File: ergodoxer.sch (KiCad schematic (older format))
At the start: 106 parts, among them J1 USB_C_Receptacle, SW1 SW_Push, SW10 SW_Push, SW11 SW_Push, SW12 SW_Push, SW13 SW_Push, SW14 SW_Push, SW15 SW_Push, SW16 SW_Push, SW17 SW_Push, SW18 SW_Push, SW19 SW_Push, SW2 SW_Push, SW20 SW_Push, SW21 SW_Push, SW22 SW_Push, SW23 SW_Push, SW24 SW_Push, SW25 SW_Push, SW26 SW_Push, SW27 SW_Push, SW28 SW_Push, SW29 SW_Push, SW3 SW_Push, SW30 SW_Push, SW31 SW_Push, SW32 SW_Push, SW33 SW_Push, SW34 SW_Push, SW35 SW_Push, SW36 SW_Push, SW37 SW_Push, SW38 SW_Push, SW39 SW_Push, SW4 SW_Push, SW40 SW_Push, SW41 SW_Push, SW43 SW_Push, SW44 SW_Push, SW45 SW_Push, SW46 SW_Push, SW47 SW_Push, SW48 SW_Push, SW49 SW_Push, SW5 SW_Push, SW50 SW_Push, SW51 SW_Push, SW52 SW_Push, SW53 SW_Push, SW6 SW_Push, SW7 SW_Push, SW8 SW_Push, SW9 SW_Push, U1 proton_c

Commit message: Flip switches upside down
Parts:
- SW1, SW10, SW11, SW12, SW13, SW14, SW15, SW16, SW17, SW18, SW19, SW2, SW20, SW21, SW22, SW23, SW24, SW25, SW26, SW27, SW28, SW29, SW3, SW30, SW31, SW32, SW33, SW34, SW35, SW36, SW37, SW38, SW39, SW4, SW40, SW41, SW43, SW44, SW45, SW46, SW47, SW48, SW49, SW5, SW50, SW51, SW52, SW53, SW6, SW7, SW8, SW9: footprint Button_Switch_keyboard:SW_Cherry_MX_1.00u_PCB -> switches:SW_Cherry_MX_1.00u_PCB_dual
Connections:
- no-connect marks 0 -> 21

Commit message: Add leds
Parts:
- added LE23, LED1, LED10, LED11, LED12, LED13, LED14, LED15, LED16, LED17, LED18, LED19, LED2, LED20, LED21, LED22, LED24, LED25, LED26, LED27, LED28, LED29, LED3, LED30, LED31, LED32, LED33, LED34, LED35, LED36, LED37, LED38, LED39, LED4, LED40, LED41, LED45, LED46, LED47, LED48, LED49, LED5, LED50, LED51, LED52, LED53, LED6, LED7, LED8, LED9: WS2812B, switches:LED_WS2812B-inverted, symbol LED:WS2812B
- added LED43, LED44: WS2812, switches:LED_WS2812B-inverted, symbol LED:WS2812B
- SW1, SW13, SW19, SW25, SW31, SW37, SW7: value SW_Push -> SW_Push_mod
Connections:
- net GND: now also LE23.3 (VSS), LED1.3 (VSS), LED10.3 (VSS), LED11.3 (VSS), LED12.3 (VSS), LED13.3 (VSS), LED14.3 (VSS), LED15.3 (VSS), LED16.3 (VSS), LED17.3 (VSS), LED18.3 (VSS), LED19.3 (VSS), LED2.3 (VSS), LED20.3 (VSS), LED21.3 (VSS), LED22.3 (VSS), LED24.3 (VSS), LED25.3 (VSS), LED26.3 (VSS), LED27.3 (VSS), LED28.3 (VSS), LED29.3 (VSS), LED3.3 (VSS), LED30.3 (VSS), LED31.3 (VSS), LED32.3 (VSS), LED33.3 (VSS), LED34.3 (VSS), LED35.3 (VSS), LED36.3 (VSS), LED37.3 (VSS), LED38.3 (VSS), LED39.3 (VSS), LED4.3 (VSS), LED40.3 (VSS), LED41.3 (VSS), LED43.3 (VSS), LED44.3 (VSS), LED45.3 (VSS), LED46.3 (VSS), LED47.3 (VSS), LED48.3 (VSS), LED49.3 (VSS), LED5.3 (VSS), LED50.3 (VSS), LED51.3 (VSS), LED52.3 (VSS), LED53.3 (VSS), LED6.3 (VSS), LED7.3 (VSS), LED8.3 (VSS), LED9.3 (VSS)
- net VBUS: now also LE23.1 (VDD), LED1.1 (VDD), LED10.1 (VDD), LED11.1 (VDD), LED12.1 (VDD), LED13.1 (VDD), LED14.1 (VDD), LED15.1 (VDD), LED16.1 (VDD), LED17.1 (VDD), LED18.1 (VDD), LED19.1 (VDD), LED2.1 (VDD), LED20.1 (VDD), LED21.1 (VDD), LED22.1 (VDD), LED24.1 (VDD), LED25.1 (VDD), LED26.1 (VDD), LED27.1 (VDD), LED28.1 (VDD), LED29.1 (VDD), LED3.1 (VDD), LED30.1 (VDD), LED31.1 (VDD), LED32.1 (VDD), LED33.1 (VDD), LED34.1 (VDD), LED35.1 (VDD), LED36.1 (VDD), LED37.1 (VDD), LED38.1 (VDD), LED39.1 (VDD), LED4.1 (VDD), LED40.1 (VDD), LED41.1 (VDD), LED43.1 (VDD), LED44.1 (VDD), LED45.1 (VDD), LED46.1 (VDD), LED47.1 (VDD), LED48.1 (VDD), LED49.1 (VDD), LED5.1 (VDD), LED50.1 (VDD), LED51.1 (VDD), LED52.1 (VDD), LED53.1 (VDD), LED6.1 (VDD), LED7.1 (VDD), LED8.1 (VDD), LED9.1 (VDD)
- net column1: now also U1.B0 (PB0); no longer U1.B1 (PB1)
- net column2: now also U1.B1 (PB1); no longer U1.B2 (PB2)
- net column3: now also U1.B2 (PB2); no longer U1.B3 (PB3)
- net column4: now also U1.B13 (PB13/SCLK); no longer U1.B7 (PB7/SDA)
- net column5: now also SW43.1, SW44.1, U1.B5 (PB5); no longer U1.B6 (PB6/SCL)
- net column6: now also SW46.1, SW47.1, U1.B4 (PB4); no longer U1.B5 (PB5)
- net column7: now also SW48.1, SW49.1, SW50.1, U1.B3 (PB3); no longer U1.B4 (PB4)
- net column8: now also SW45.1, SW51.1, SW52.1, SW53.1, U1.B10 (PB10); no longer SW43.1, SW44.1, U1.A7 (PA7)
- net row4: no longer D45.1 (K), D48.1 (K), D51.1 (K)
- net row5: now also D45.1 (K), U1.A4 (PA4/SPEAKER1); no longer D43.1 (K), D46.1 (K), D49.1 (K), D52.1 (K), U1.B9 (PB9)
- net row6: now also D48.1 (K), D51.1 (K), U1.A5 (PA5/SPEAKER2); no longer D44.1 (K), D47.1 (K), D50.1 (K), D53.1 (K), U1.B11 (PB11)
- net row7: now reaches U1.B12 (PB12)
- net row7: now also D43.1 (K), D46.1 (K), D49.1 (K), D52.1 (K)
- net SDA: now reaches J1.A5 (CC1), J1.A8 (SBU1)
- net SDA: now also U1.B7 (PB7/SDA); no longer U1.B13 (PB13/SCLK)
- net SCL: now reaches J1.A6 (D+), J1.A7 (D-)
- net SCL: now also U1.B6 (PB6/SCL); no longer U1.B15 (PB15/MOSI)
- removed net column10: SW48.1, SW49.1, SW50.1, U1.A5 (PA5/SPEAKER2)
- removed net column11: SW51.1, SW52.1, SW53.1, U1.A4 (PA4/SPEAKER1)
- removed net column9: SW45.1, SW46.1, SW47.1, U1.A6 (PA6)
- new net: LED43.4 (DIN), LED44.2 (DOUT)
- new net: LED44.4 (DIN), LED47.2 (DOUT)
- new net: LED19.4 (DIN), LED25.2 (DOUT)
- new net: LED25.4 (DIN), LED31.2 (DOUT)
- new net: LED26.2 (DOUT), LED32.4 (DIN)
- new net: LED20.2 (DOUT), LED26.4 (DIN)
- new net: LED21.4 (DIN), LED27.2 (DOUT)
- new net: LED27.4 (DIN), LED33.2 (DOUT)
- new net: LE23.4 (DIN), LED29.2 (DOUT)
- new net: LED29.4 (DIN), LED35.2 (DOUT)
- new net: LED30.2 (DOUT), LED36.4 (DIN)
- new net: LED24.2 (DOUT), LED30.4 (DIN)
- new net: LED31.4 (DIN), LED37.2 (DOUT)
- new net: LED32.2 (DOUT), LED38.4 (DIN)
- new net: LED33.4 (DIN), LED39.2 (DOUT)
- new net: LED35.4 (DIN), LED41.2 (DOUT)
- new net: LED36.2 (DOUT), LED45.4 (DIN)
- new net: LED38.2 (DOUT), LED39.4 (DIN)
- new net: LED40.2 (DOUT), LED41.4 (DIN)
- new net: LED13.4 (DIN), LED19.2 (DOUT)
- new net: LED14.2 (DOUT), LED20.4 (DIN)
- new net: LED15.4 (DIN), LED21.2 (DOUT)
- new net: LE23.2 (DOUT), LED17.4 (DIN)
- new net: LED18.2 (DOUT), LED24.4 (DIN)
- new net: LED13.2 (DOUT), LED7.4 (DIN)
- new net: LED14.4 (DIN), LED8.2 (DOUT)
- new net: LED15.2 (DOUT), LED9.4 (DIN)
- new net: LED11.4 (DIN), LED17.2 (DOUT)
- new net: LED12.2 (DOUT), LED18.4 (DIN)
- new net: LED1.2 (DOUT), LED2.4 (DIN)
- new net: LED1.4 (DIN), LED7.2 (DOUT)
- new net: LED2.2 (DOUT), LED8.4 (DIN)
- new net: LED3.2 (DOUT), LED4.4 (DIN)
- new net: LED3.4 (DIN), LED9.2 (DOUT)
- new net: LED5.2 (DOUT), LED6.4 (DIN)
- new net: LED11.2 (DOUT), LED5.4 (DIN)
- new net: LED12.4 (DIN), LED6.2 (DOUT)
- new net: LED45.2 (DOUT), LED48.4 (DIN)
- new net: LED48.2 (DOUT), LED51.4 (DIN)
- new net: LED51.2 (DOUT), LED52.4 (DIN)
- new net: LED52.2 (DOUT), LED53.4 (DIN)
- new net: LED50.4 (DIN), LED53.2 (DOUT)
- new net: LED49.4 (DIN), LED50.2 (DOUT)
- new net: LED46.4 (DIN), LED49.2 (DOUT)
- new net: LED46.2 (DOUT), LED47.4 (DIN)
- new net LED_IN: U1.B15 (PB15/MOSI)
- new net ledinput: LED37.4 (DIN)
- new net row8: D44.1 (K), D47.1 (K), D50.1 (K), D53.1 (K), U1.B11 (PB11)
- now unconnected: J1.B6 (D+), J1.B7 (D-), U1.B14 (PB14/MISO)
- no-connect marks 21 -> 17
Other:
- moved on the sheet: D43, D44, D45, D46, D47, D48, D49, D50, D51, D52, D53, SW43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

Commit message: WIP update to square led holes
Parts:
- removed D36: 1N4148, Diodes_ThroughHole:D_DO-35_SOD27_P7.62mm_Horizontal, symbol Diode:1N4148
- removed LED36: WS2812B, switches:LED_WS2812B-inverted, symbol LED:WS2812B
- removed SW36: SW_Push, switches:SW_Cherry_MX_1.00u_PCB_dual, symbol Switch:SW_Push
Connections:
- net column6: now also SW45.1
- net column8: no longer SW45.1
- net row5: no longer D45.1 (K)
- net row6: now also D45.1 (K)
- net at LED28.2 (DOUT): now also LED34.4 (DIN)
- net at LED28.4 (DIN): now also LED22.2 (DOUT)
- net at LED30.2 (DOUT): now also LED45.4 (DIN)
- net at LED34.2 (DOUT): now also LED40.4 (DIN)
- net at LED22.4 (DIN): now also LED16.2 (DOUT)
- net at LED16.4 (DIN): now also LED10.2 (DOUT)
- net at LED4.2 (DOUT): now also LED10.4 (DIN)
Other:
- moved on the sheet: D45, SW45
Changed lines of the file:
@@
-	0    -1   -1   0
-$EndComp
-$Comp
-L Switch:SW_Push SW36
-U 1 1 5C72915C
-P 5450 5600
-F 0 "SW36" H 5450 5885 50  0000 C CNN
-F 1 "SW_Push" H 5450 5794 50  0000 C CNN
-F 2 "switches:SW_Cherry_MX_1.00u_PCB_dual" H 5450 5800 50  0001 C CNN
-F 3 "" H 5450 5800 50  0001 C CNN
-	1    5450 5600
-	1    0    0    -1
-$EndComp
-$Comp
-L Diode:1N4148 D36
-U 1 1 5C729163
-P 5650 5750
-F 0 "D36" H 5650 5850 50  0000 C CNN
-F 1 "1N4148" H 5650 5650 50  0000 C CNN
-F 2 "Diodes_ThroughHole:D_DO-35_SOD27_P7.62mm_Horizontal" H 5650 5575 50  0001 C CNN
-F 3 "http://www.nxp.com/documents/data_sheet/1N4148_1N4448.pdf" H 5650 5750 50  0001 C CNN
-	1    5650 5750
 	0    -1   -1   0
 $EndComp
@@
 Connection ~ 4250 5900
 Wire Wire Line
-	4950 5900 5650 5900
-Connection ~ 4950 5900
-Wire Wire Line
 	3150 4800 3150 5600
 Wire Wire Line
@@
 Wire Wire Line
 	4550 4800 4550 5600
-Wire Wire Line
-	5250 4800 5250 5600
 Wire Wire Line
 	2450 4800 2450 5600
@@
 Connection ~ 3850 4800
 Connection ~ 4550 4800
-Connection ~ 5250 4800
 $Comp
 L Switch:SW_Push SW45
 U 1 1 5C75EE71
-P 4700 6650
-F 0 "SW45" H 4700 6935 50  0000 C CNN
-F 1 "SW_Push" H 4700 6844 50  0000 C CNN
-F 2 "switches:SW_Cherry_MX_1.00u_PCB_dual" H 4700 6850 50  0001 C CNN
-F 3 "" H 4700 6850 50  0001 C CNN
-	1    4700 6650
+P 4700 6800
+F 0 "SW45" H 4700 7085 50  0000 C CNN
+F 1 "SW_Push" H 4700 6994 50  0000 C CNN
+F 2 "switches:SW_Cherry_MX_1.00u_PCB_dual" H 4700 7000 50  0001 C CNN
+F 3 "" H 4700 7000 50  0001 C CNN
+	1    4700 6800
 	1    0    0    -1
 $EndComp
@@
 L Diode:1N4148 D45
 U 1 1 5C75EE78
-P 4900 6800
-F 0 "D45" H 4900 6900 50  0000 C CNN
-F 1 "1N4148" H 4900 6700 50  0000 C CNN
-F 2 "Diodes_ThroughHole:D_DO-35_SOD27_P7.62mm_Horizontal" H 4900 6625 50  0001 C CNN
-F 3 "http://www.nxp.com/documents/data_sheet/1N4148_1N4448.pdf" H 4900 6800 50  0001 C CNN
-	1    4900 6800
+P 4900 6950
+F 0 "D45" H 4900 7050 50  0000 C CNN
+F 1 "1N4148" H 4900 6850 50  0000 C CNN
+F 2 "Diodes_ThroughHole:D_DO-35_SOD27_P7.62mm_Horizontal" H 4900 6775 50  0001 C CNN
+F 3 "http://www.nxp.com/documents/data_sheet/1N4148_1N4448.pdf" H 4900 6950 50  0001 C CNN
+	1    4900 6950
 	0    -1   -1   0
 $EndComp
@@
 row6
 Wire Wire Line
-	3500 7100 5600 7100
-Text GLabel 4500 7500 1    50   Input ~ 0
+	3500 7100 4900 7100
+Text GLabel 4500 6550 1    50   Input ~ 0
 column6
-Wire Wire Line
-	4500 7500 4500 7600
 Connection ~ 4500 7600
-Text GLabel 4500 6400 1    50   Input ~ 0
-column8
-Wire Wire Line
-	4500 6400 4500 6650
-Text GLabel 4450 6950 0    50   Input ~ 0
-row5
-Wire Wire Line
-	4450 6950 4900 6950
+Wire Wire Line
+	4500 6550 4500 6800
 Wire Wire Line
 	7950 3350 8100 3350
@@
 	1    -2800 4700
 	-1   0    0    1
-$EndComp
-$Comp
-L LED:WS2812B LED36
-U 1 1 5CDF1437
-P -2800 5750
-F 0 "LED36" H -2459 5796 50  0000 L CNN
-F 1 "WS2812B" H -2459 5705 50  0000 L CNN
-F 2 "switches:LED_WS2812B-inverted" H -2750 5450 50  0001 L TNN
-F 3 "https://cdn-shop.adafruit.com/datasheets/WS2812B.pdf" H -2700 5375 50  0001 L TNN
-	1    -2800 5750
-	1    0    0    -1
 $EndComp
 $Comp
@@
 	-4750 5750 -4300 5750
 Wire Wire Line
-	-3700 5750 -3100 5750
-Wire Wire Line
 	-1550 5000 -1550 5200
 Wire Wire Line
@@
 	-2800 5200 -4000 5200
 Wire Wire Line
-	-2800 5200 -2800 5450
-Wire Wire Line
 	-1550 3900 -1550 4100
 Wire Wire Line
@@
 Wire Wire Line
 	-9150 3600 -8950 3600
-Wire Wire Line
-	-2500 5750 -1550 5750
 $Comp
 L power:GND #PWR0107
@@
 	-8650 6450 -8650 6050
 Wire Wire Line
-	-2800 6050 -2800 6450
-Wire Wire Line
 	-7450 6050 -7450 6450
 Wire Wire Line
@@
 	-5050 6450 -4000 6450
 Connection ~ -4000 6450
-Wire Wire Line
-	-4000 6450 -2800 6450
 Wire Wire Line
 	-4000 6050 -4000 6450
@@
 Connection ~ 3800 7600
 $Comp
-L power:GND #PWR?
+L power:GND #PWR0128
 U 1 1 5C754416
-P -2800 6450
-F 0 "#PWR?" H -2800 6200 50  0001 C CNN
-F 1 "GND" V -2795 6322 50  0000 R CNN
-F 2 "" H -2800 6450 50  0001 C CNN
-F 3 "" H -2800 6450 50  0001 C CNN
-	1    -2800 6450
-	1    0    0    -1
-$EndComp
-Connection ~ -2800 6450
+P -4000 6450
+F 0 "#PWR0128" H -4000 6200 50  0001 C CNN
+F 1 "GND" V -3995 6322 50  0000 R CNN
+F 2 "" H -4000 6450 50  0001 C CNN
+F 3 "" H -4000 6450 50  0001 C CNN
+	1    -4000 6450
+	1    0    0    -1
+$EndComp
+Wire Wire Line
+	-3700 5750 -1550 5750
+Wire Wire Line
+	-8350 3600 -7750 3600
+Wire Wire Line
+	-7150 3600 -6550 3600
+Wire Wire Line
+	-5950 3600 -5350 3600
+Wire Wire Line
+	-4750 3600 -4300 3600
+Wire Wire Line
+	-3700 3600 -3100 3600
+Wire Wire Line
+	-1850 3600 -2500 3600
+Connection ~ 4900 7100
+Wire Wire Line
+	4900 7100 5600 7100
+Wire Wire Line
+	4500 6800 4500 7600
+Connection ~ 4500 6800
 $EndSCHEMATC

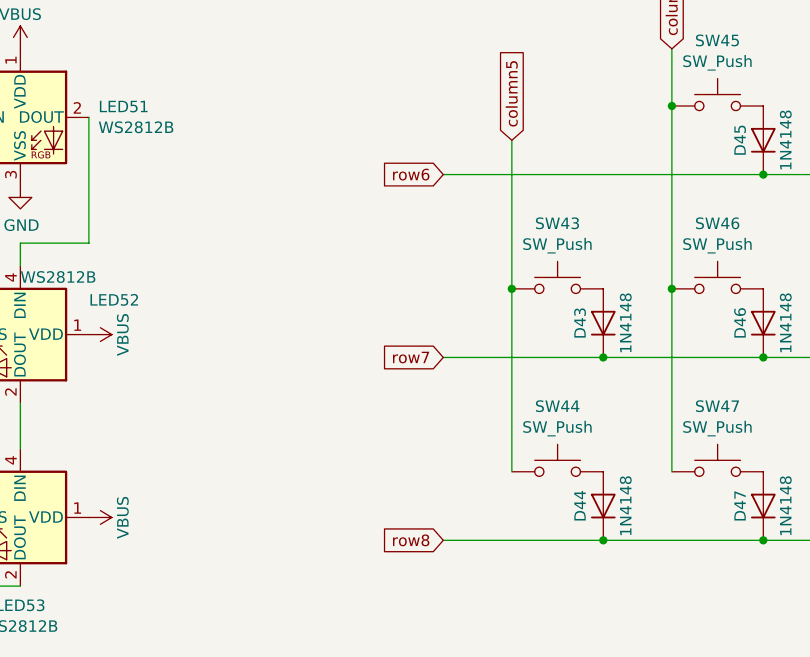
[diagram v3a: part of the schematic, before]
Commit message: Add qmk hardware as a submodule and connect thumb cluster
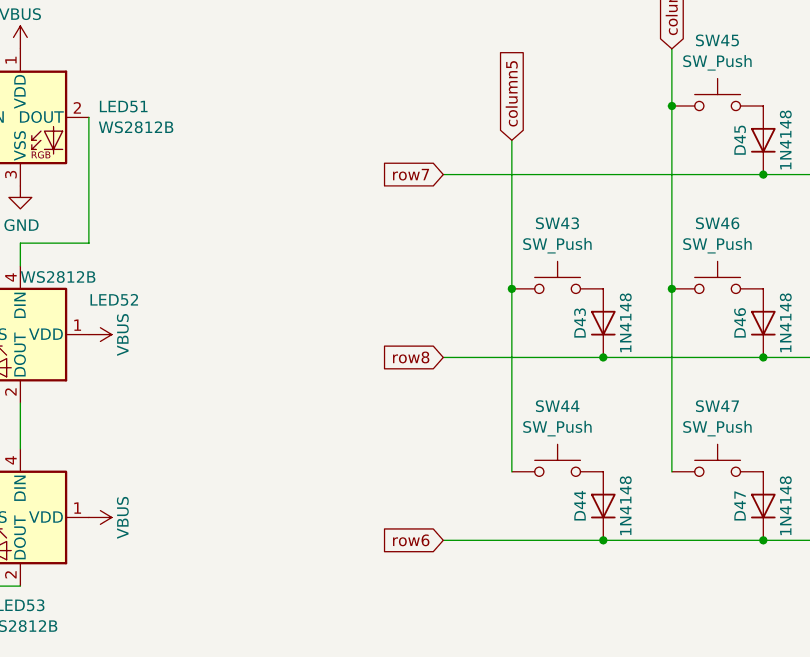
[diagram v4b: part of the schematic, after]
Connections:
- net row6: now also D44.1 (K), D47.1 (K), D50.1 (K), D53.1 (K); no longer D45.1 (K), D48.1 (K), D51.1 (K)
- net row7: now also D45.1 (K), D48.1 (K), D51.1 (K); no longer D43.1 (K), D46.1 (K), D49.1 (K), D52.1 (K)
- net row8: now also D43.1 (K), D46.1 (K), D49.1 (K), D52.1 (K); no longer D44.1 (K), D47.1 (K), D50.1 (K), D53.1 (K)
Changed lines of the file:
@@
 EESchema Schematic File Version 4
-LIBS:ergodoxer-cache
 EELAYER 26 0
 EELAYER END
@@
 Connection ~ 5600 7900
 Connection ~ 5600 8700
-Text GLabel 3500 8700 0    50   Input ~ 0
+Text GLabel 3500 7900 0    50   Input ~ 0
 row8
-Text GLabel 3500 7900 0    50   Input ~ 0
+Text GLabel 3500 7100 0    50   Input ~ 0
 row7
 Connection ~ 5900 6800
@@
 	5200 6400 5200 6800
 Connection ~ 5200 6800
-Text GLabel 3500 7100 0    50   Input ~ 0
+Text GLabel 3500 8700 0    50   Input ~ 0
 row6
 Wire Wire Line

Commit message: Redo thumb cluster
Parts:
- removed D44, D47: 1N4148, Diodes_ThroughHole:D_DO-35_SOD27_P7.62mm_Horizontal, symbol Diode:1N4148
- removed LED44: WS2812, switches:LED_WS2812B-inverted, symbol LED:WS2812B
- removed LED47: WS2812B, switches:LED_WS2812B-inverted, symbol LED:WS2812B
- removed SW44, SW47: SW_Push, switches:SW_Cherry_MX_1.00u_PCB_dual, symbol Switch:SW_Push
- SW43, SW46: footprint switches:SW_Cherry_MX_1.00u_PCB_dual -> switches:SW_Cherry_MX_2.00u_PCB_reversible
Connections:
- net GND: now also J1.S1 (SHIELD)
- net column4: now also U1.B8 (PB8); no longer U1.B13 (PB13/SCLK)
- net column8: now also U1.A7 (PA7); no longer U1.B10 (PB10)
- net row3: now also U1.B13 (PB13/SCLK); no longer U1.A0 (PA0)
- net row4: now also U1.A15 (PA15); no longer U1.B8 (PB8)
- net row5: now also U1.A8 (PA8); no longer U1.A4 (PA4/SPEAKER1)
- net row6: now also U1.A4 (PA4/SPEAKER1); no longer U1.A5 (PA5/SPEAKER2)
- net row7: now also U1.A5 (PA5/SPEAKER2); no longer U1.B12 (PB12)
- net row8: now also U1.A6 (PA6); no longer U1.B11 (PB11)
- net at LED43.2 (DOUT): now also LED50.4 (DIN)
- net at LED43.4 (DIN): now also LED46.2 (DOUT)
- net at LED52.2 (DOUT): now also LED49.4 (DIN); no longer LED53.4 (DIN)
- net at LED53.2 (DOUT): no longer LED50.4 (DIN)
- net at LED50.2 (DOUT): now also LED53.4 (DIN); no longer LED49.4 (DIN)
- no-connect marks 17 -> 15
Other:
- moved on the sheet: LED43, LED46, LED49

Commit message: Change microcontroller to neutron c
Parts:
- removed J1: USB_C_Receptacle, Connectors_USB:USB_C_Receptacle_GCT_USB4085, symbol Connector:USB_C_Receptacle
- removed U1: proton_c, protonc:proton_c, symbol proton_c:proton_c
- added J1: USB_C_Receptacle_USB2.0, Connectors_USB:USB_C_Receptacle_GCT_USB4085, symbol Connector:USB_C_Receptacle_USB2.0
- added JP1, JP2, JP3, JP4: SolderJumper_3_Open, Jumper:SolderJumper-3_P1.3mm_Open_Pad1.0x1.5mm, symbol Jumper:SolderJumper_3_Open
- added U1: neutron-c, neutron-c:neutron-c, symbol neutron_c_lib:neutron-c
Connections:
- net labels added: CC, D+, D-, SBU, miso1, mosi1, sclk1, uart1_rx, uart1_tx, uart3_rx, uart3_tx
- net labels removed: LED_IN, SCL, SDA
- wire segments 312 -> 320
- no-connect marks 15 -> 2
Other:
- note added: "Does keebr support multiple GPIO ports for rows/cols?"
- note added: "LED capacitors"
- note added: "TODO:"
